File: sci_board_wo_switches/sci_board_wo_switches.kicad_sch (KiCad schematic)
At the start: 18 parts

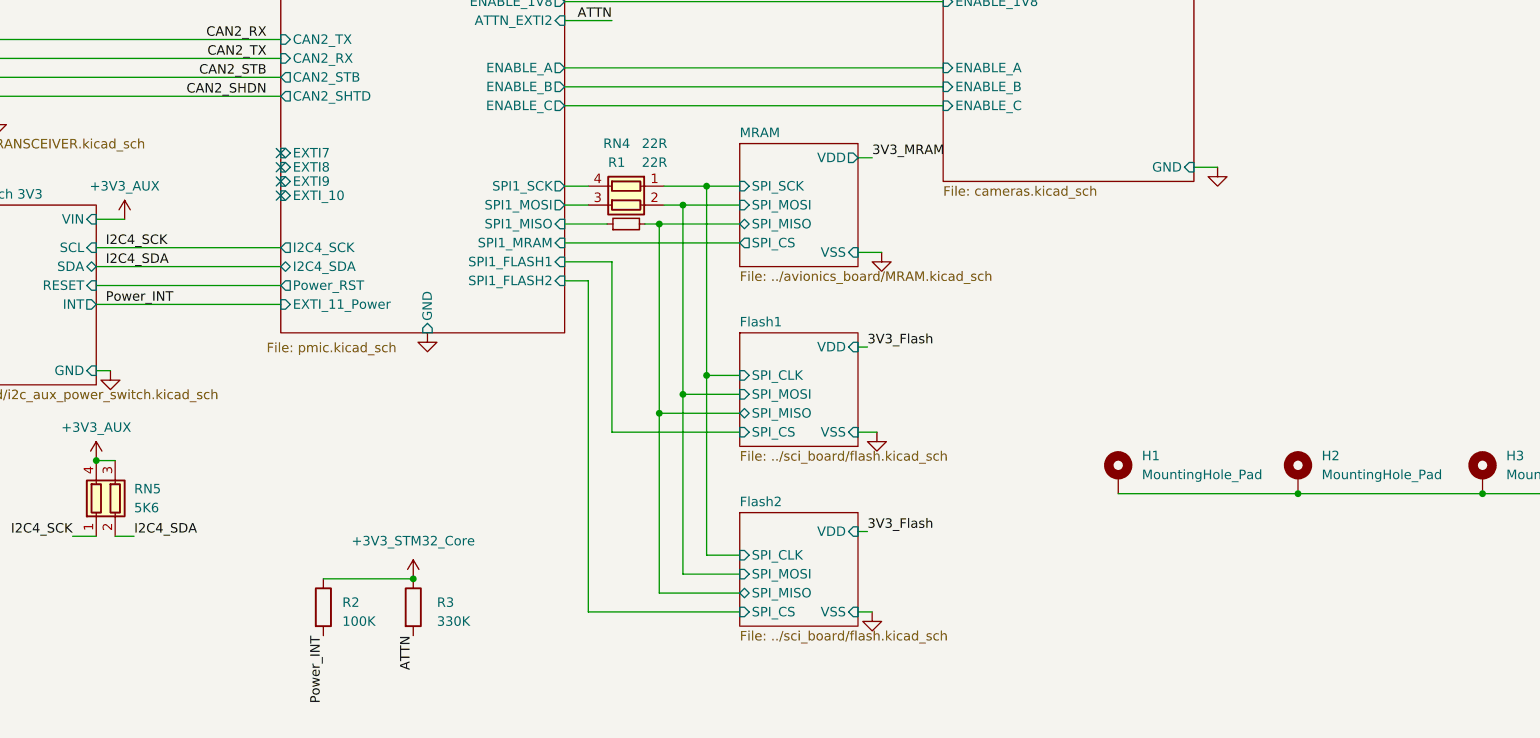
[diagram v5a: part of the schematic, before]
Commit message: move SPI CS pullups to outer schema to combine multiple with RNs
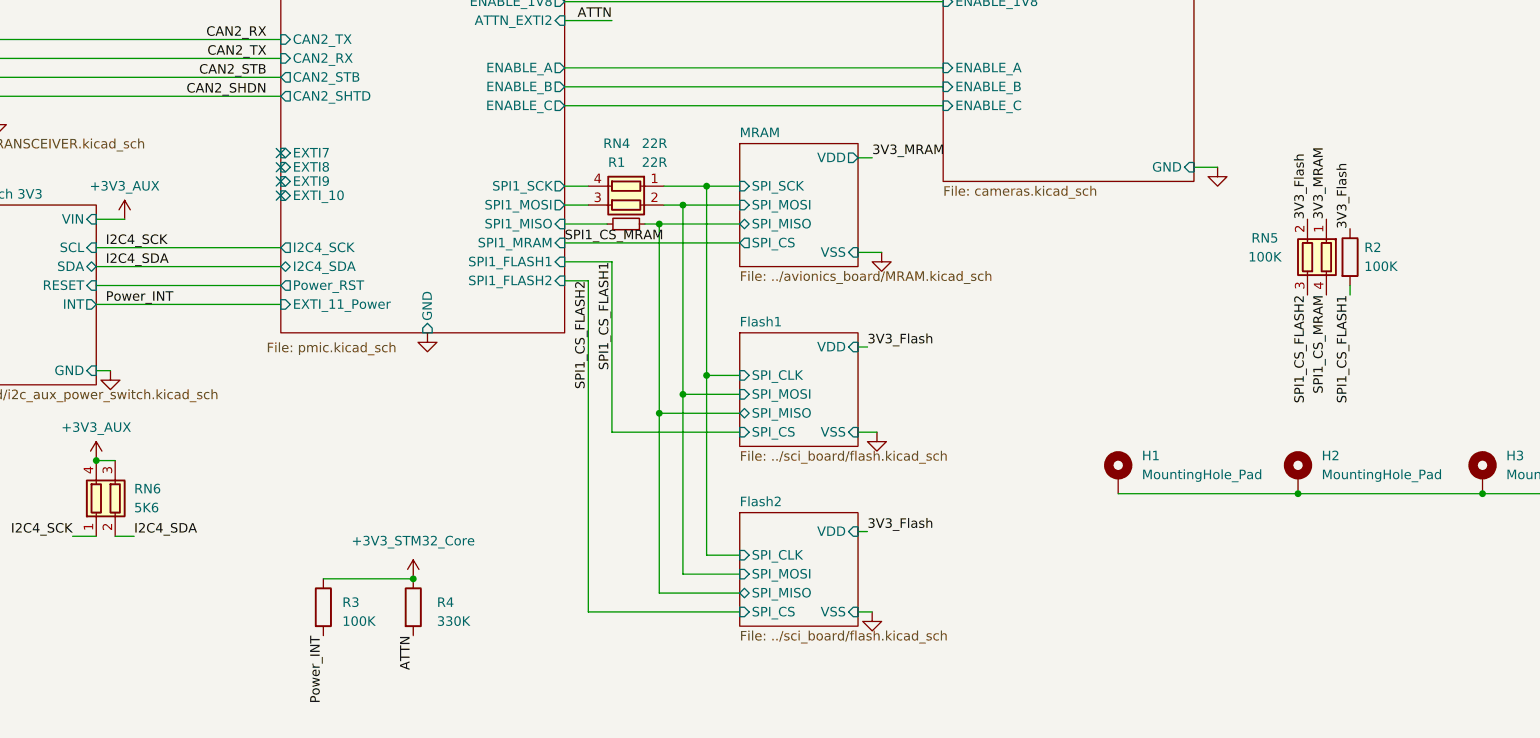
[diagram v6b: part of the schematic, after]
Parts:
- added R2: 100K, Resistor_SMD:R_0402_1005Metric_Pad0.72x0.64mm_HandSolder, symbol Device:R
- added RN5: 100K, Common:R_Array_Convex_2x0402_widepads, symbol Device:R_Pack02
- renumbered R2 to R3, R3 to R4, RN5 to RN6
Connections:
- net 3V3_Flash: now also R2.1, RN5.2 (R2.1)
- net 3V3_MRAM: now also RN5.1 (R1.1)
- new net SPI1_CS_FLASH1: R2.2
- new net SPI1_CS_FLASH2: RN5.3 (R2.2)
- new net SPI1_CS_MRAM: RN5.4 (R1.2)

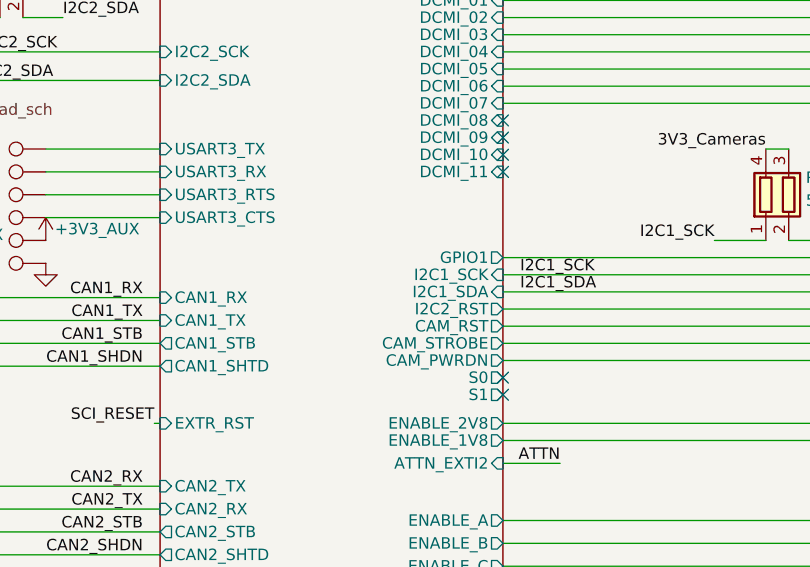
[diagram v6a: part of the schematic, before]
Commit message: SCI bodge board to correct I2C switching
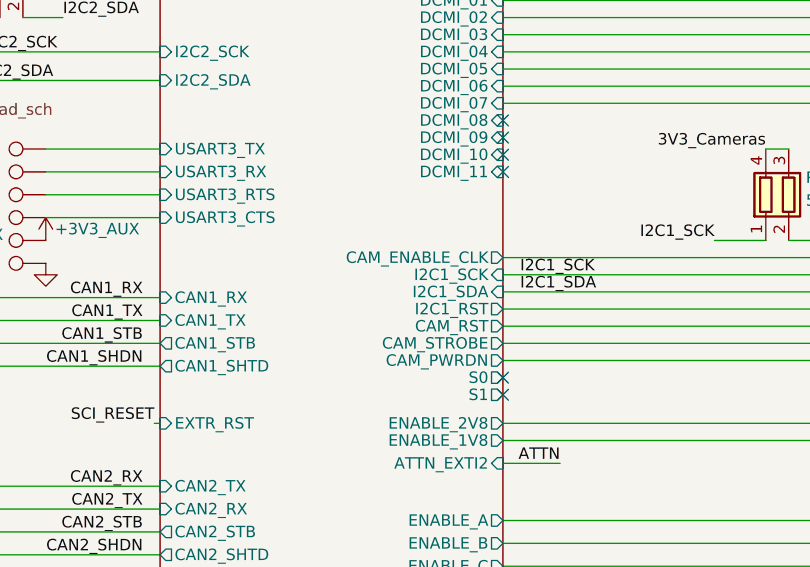
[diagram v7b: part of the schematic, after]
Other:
- sheet PMIC ports: added CAM_ENABLE_CLK, I2C1_RST; removed GPIO1, I2C2_RST
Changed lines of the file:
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@@
-			)
-		)
-		(pin "GPIO1" output
-			(at 126.365 76.2 0)
-			(effects
-				(font
-					(size 1.27 1.27)
-				)
-				(justify right)
 			)
 		)
@@
 			)
 		)
-		(pin "I2C2_RST" output
+		(pin "I2C1_RST" output
 			(at 126.365 81.915 0)
 			(effects
 				(font
+					(size 1.27 1.27)
+				)
+				(justify right)
+			)
+		)
+		(pin "CAM_ENABLE_CLK" output
+			(at 126.365 76.2 0)
+			(effects
+				(font

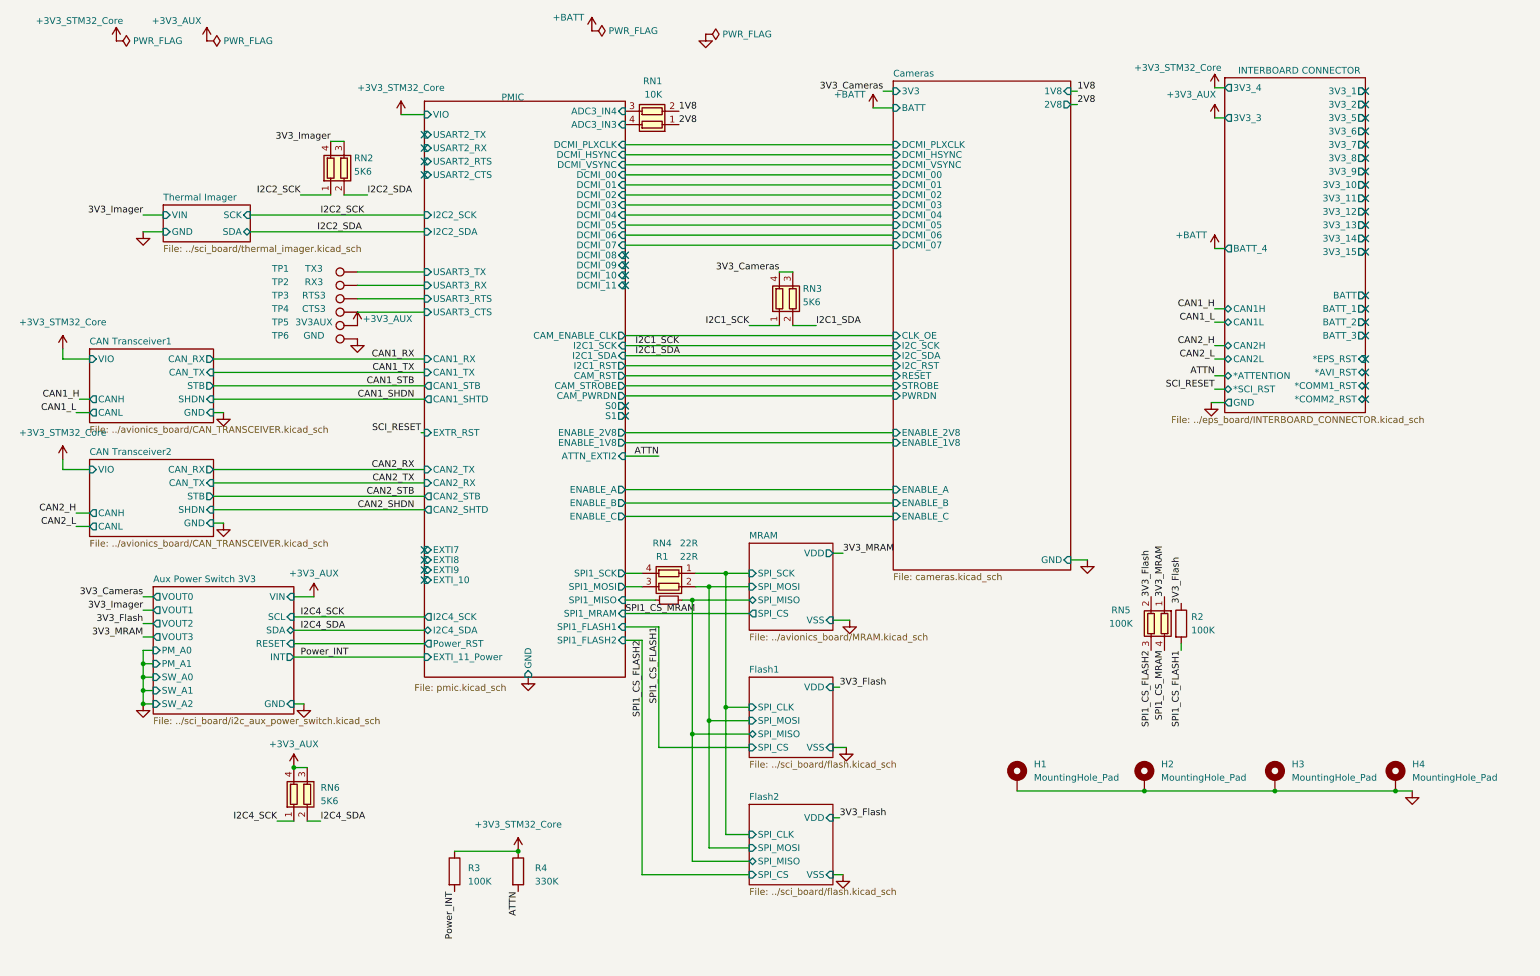
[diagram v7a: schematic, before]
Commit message: absolute paths for includes of includes or the second level common/sheet will cause problems!
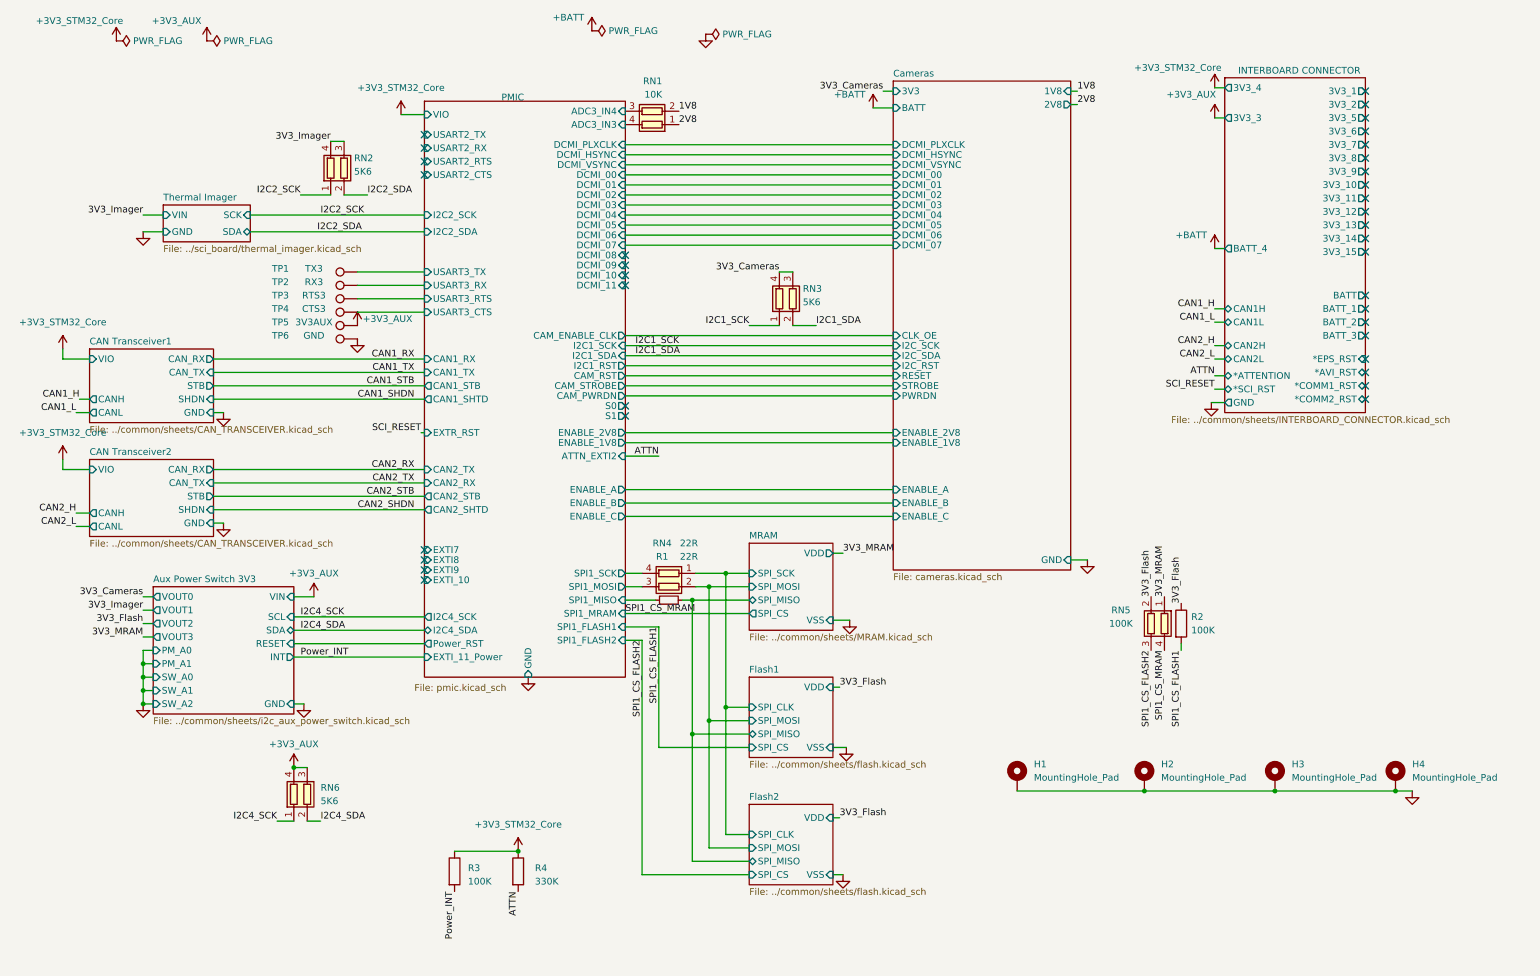
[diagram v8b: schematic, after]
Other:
- sheet Aux Power Switch 3V3: file ../sci_board/i2c_aux_power_switch.kicad_sch -> ../common/sheets/i2c_aux_power_switch.kicad_sch
- sheet CAN Transceiver1: file ../avionics_board/CAN_TRANSCEIVER.kicad_sch -> ../common/sheets/CAN_TRANSCEIVER.kicad_sch
- sheet CAN Transceiver2: file ../avionics_board/CAN_TRANSCEIVER.kicad_sch -> ../common/sheets/CAN_TRANSCEIVER.kicad_sch
- sheet Flash1: file ../sci_board/flash.kicad_sch -> ../common/sheets/flash.kicad_sch
- sheet Flash2: file ../sci_board/flash.kicad_sch -> ../common/sheets/flash.kicad_sch
- sheet INTERBOARD CONNECTOR: file ../eps_board/INTERBOARD_CONNECTOR.kicad_sch -> ../common/sheets/INTERBOARD_CONNECTOR.kicad_sch
- sheet MRAM: file ../avionics_board/MRAM.kicad_sch -> ../common/sheets/MRAM.kicad_sch
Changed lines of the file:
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@@
 			)
 		)
-		(property "Sheetfile" "../avionics_board/CAN_TRANSCEIVER.kicad_sch"
+		(property "Sheetfile" "../common/sheets/CAN_TRANSCEIVER.kicad_sch"
 			(at 24.765 93.2946 0)
 			(effects
@@
 			)
 		)
-		(property "Sheetfile" "../sci_board/flash.kicad_sch"
+		(property "Sheetfile" "../common/sheets/flash.kicad_sch"
 			(at 149.86 180.9246 0)
 			(effects
@@
 			)
 		)
-		(property "Sheetfile" "../avionics_board/CAN_TRANSCEIVER.kicad_sch"
+		(property "Sheetfile" "../common/sheets/CAN_TRANSCEIVER.kicad_sch"
 			(at 24.765 114.8846 0)
 			(effects
@@
 			)
 		)
-		(property "Sheetfile" "../eps_board/INTERBOARD_CONNECTOR.kicad_sch"
+		(property "Sheetfile" "../common/sheets/INTERBOARD_CONNECTOR.kicad_sch"
 			(at 229.87 91.44 0)
 			(effects
@@
 			)
 		)
-		(property "Sheetfile" "../sci_board/i2c_aux_power_switch.kicad_sch"
+		(property "Sheetfile" "../common/sheets/i2c_aux_power_switch.kicad_sch"
 			(at 36.83 148.5396 0)
 			(effects
@@
 			)
 		)
-		(property "Sheetfile" "../avionics_board/MRAM.kicad_sch"
+		(property "Sheetfile" "../common/sheets/MRAM.kicad_sch"
 			(at 149.86 132.6646 0)
 			(effects
@@
 			)
 		)
-		(property "Sheetfile" "../sci_board/flash.kicad_sch"
+		(property "Sheetfile" "../common/sheets/flash.kicad_sch"
 			(at 149.86 156.7946 0)
 			(effects
